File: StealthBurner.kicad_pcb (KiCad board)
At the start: 2 copper layers, 44.9 x 31.7 mm, 14 parts, among them J1 PROBE, J2 E-Step, J3 HE, J4 HET, J5 FS, J6 HEF, J7 PCF, J8 LED, J9 MCU, M1 Mount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

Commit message: 修改设计规范
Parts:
- moved J1 2.13 mm to (154.1, 107.2)
- moved D1 0.43 mm to (151.3, 102.7)
- moved G*** 0.25 mm to (152.7, 98.6)
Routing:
- net +24V: track 18.6 -> 16.4 mm
- net /HET: track 43.3 -> 44.3 mm
- net GNDA: track 56.3 -> 57.3 mm
- net /A-: track 8.05 -> 7.49 mm

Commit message: 重新设计 PCB
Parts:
- D1: footprint Diode_THT:D_DO-34_SOD68_P2.54mm_Vertical_AnodeUp -> Diode_THT:D_DO-35_SOD27_P2.54mm_Vertical_AnodeUp
- M1, M2: value Mount -> M3_hole; footprint MountingHole:MountingHole_3.2mm_M3_ISO7380_Pad -> MountingHole:MountingHole_3.2mm_M3_User
- moved J1 20.4 mm to (136.3, 97.3), turned to -90 degrees
- moved M1 19.7 mm to (148.0, 99.2)
- moved M2 15.3 mm to (136.0, 112.0)
- moved J3 14.9 mm to (152.6, 106.1), turned to 90 degrees
- moved D1 11.6 mm to (139.9, 100.4), turned to 90 degrees
- moved G*** 1.74 mm to (154.2, 97.8)
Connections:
- J9 pad 14: /P_SIG -> /HE-
- J9 pad 15: /FS -> /HE+
- J9 pad 4: /HE- -> /P_SIG
- J9 pad 5: /HE+ -> /FS
- J9 pad 8: /HEF -> /PCF
- J9 pad 9: /PCF -> /HEF
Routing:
- net /HEF: track 79.6 -> 37.0 mm
- net /PCF: track 68.6 -> 36.5 mm, vias 1 -> 0
- net /HE-: track 26.8 -> 3.26 mm
- net /P_SIG: track 5.35 -> 25.1 mm
- net /HE+: track 25.4 -> 6.37 mm
- net /DATA: track 57.6 -> 40.6 mm
- net /V_FAN: track 47.4 -> 64.1 mm
- net +24V: track 16.4 -> 26.9 mm
- net /HET: track 44.3 -> 36.9 mm
- net +5V: track 39.9 -> 32.9 mm
- net /FS: track 33.2 -> 37.9 mm
- net /CBT: track 36.1 -> 40.6 mm, vias 0 -> 2
- net GNDA: track 57.3 -> 55.3 mm
- net Net-(D1-Pad1): track 4.87 -> 4.08 mm
- net GND: vias 10 -> 0
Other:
- board size 44.9 x 31.7 mm -> 45 x 31.5 mm
- board text removed: "CBT"
- board text removed: "Controller"
- board text removed: "E-STEP"
- board text removed: "FS"
- board text removed: "HE"
- board text removed: "HEF"
- board text removed: "HET"
- board text removed: "NEO"
- board text removed: "PCF"
- board text removed: "PROBE"

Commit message: 更新到 Beta2
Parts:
- moved G*** 1.25 mm to (153.0, 98.0)
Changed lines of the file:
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@@
     (title "StealthBurner Toolhead PCB")
     (date "2022-05-24")
-    (rev "Bata0")
+    (rev "Bata1")
     (company "LassiCat Organization")
     (comment 1 "Auther: CharlieYu")
@@
     (property "Sheetname" "")
     (attr smd)
-    (fp_text reference "TH1" (at 0 1.75874) (layer "F.SilkS")
+    (fp_text reference "TH1" (at -3.082812 0.004398) (layer "F.SilkS")
       (effects (font (size 1 1) (thickness 0.15)))
     )
@@
     (property "Sheetname" "")
     (attr through_hole)
-    (fp_text reference "D1" (at 0.41 1.8 90) (layer "F.SilkS")
+    (fp_text reference "D1" (at -2.2 0) (layer "F.SilkS")
       (effects (font (size 1 1) (thickness 0.15)))
     )
@@
       (effects (font (size 1 1) (thickness 0.15)))
     )
-    (fp_text user "A" (at 4.34 0 90) (layer "F.SilkS")
-      (effects (font (size 1 1) (thickness 0.15)))
-    )
-    (fp_text user "A" (at 4.34 0 90) (layer "F.Fab")
-      (effects (font (size 1 1) (thickness 0.15)))
-    )
-    (fp_text user "${REFERENCE}" (at 1.27 -2.326371 90) (layer "F.Fab")
+    (fp_text user "A" (at 4.34 0 90) (layer "F.SilkS") hide
+      (effects (font (size 1 1) (thickness 0.15)))
+    )
+    (fp_text user "A" (at 4.34 0 90) (layer "F.Fab") hide
+      (effects (font (size 1 1) (thickness 0.15)))
+    )
+    (fp_text user "${REFERENCE}" (at 1.27 -2.326371 90) (layer "F.Fab") hide
       (effects (font (size 1 1) (thickness 0.15)))
     )
@@
     (tags "mounting hole 3.2mm no annular m3")
     (attr exclude_from_pos_files exclude_from_bom)
-    (fp_text reference "M2" (at 0 -4.2) (layer "F.SilkS")
-      (effects (font (size 1 1) (thickness 0.15)))
-    )
-    (fp_text value "M3_hole" (at 0 4.2) (layer "F.Fab")
-      (effects (font (size 1 1) (thickness 0.15)))
-    )
-    (fp_text user "${REFERENCE}" (at 0 0) (layer "F.Fab")
-      (effects (font (size 1 1) (thickness 0.15)))
-    )
-    (fp_circle (center 0 0) (end 2.54 0) (layer "Cmts.User") (width 0.15) (fill none))
-    (fp_circle (center 0 0) (end 2.54 0) (layer "F.CrtYd") (width 0.05) (fill none))
+    (fp_text reference "M2" (at 0 -4.2) (layer "F.SilkS") hide
+      (effects (font (size 1 1) (thickness 0.15)))
+    )
+    (fp_text value "M3_hole" (at 0 4.2) (layer "F.Fab") hide
+      (effects (font (size 1 1) (thickness 0.15)))
+    )
+    (fp_text user "${REFERENCE}" (at 0 0) (layer "F.Fab") hide
+      (effects (font (size 1 1) (thickness 0.15)))
+    )
+    (fp_circle (center 0 0) (end 2.05 0) (layer "F.SilkS") (width 0.75) (fill none))
+    (fp_circle (center 0 0) (end 1.6 0) (layer "Cmts.User") (width 0.1) (fill none))
+    (fp_circle (center 0 0) (end 1.6 0) (layer "F.CrtYd") (width 0.1) (fill none))
     (pad "" np_thru_hole circle (at 0 0) (size 3.2 3.2) (drill 3.2) (layers *.Cu *.Mask))
   )
@@
     (tags "mounting hole 3.2mm no annular m3")
     (attr exclude_from_pos_files exclude_from_bom)
-    (fp_text reference "M1" (at 0 -4.2) (layer "F.SilkS")
-      (effects (font (size 1 1) (thickness 0.15)))
-    )
-    (fp_text value "M3_hole" (at 0 4.2) (layer "F.Fab")
-      (effects (font (size 1 1) (thickness 0.15)))
-    )
-    (fp_text user "${REFERENCE}" (at 0 0) (layer "F.Fab")
-      (effects (font (size 1 1) (thickness 0.15)))
-    )
-    (fp_circle (center 0 0) (end 2.54 0) (layer "Cmts.User") (width 0.15) (fill none))
-    (fp_circle (center 0 0) (end 2.54 0) (layer "F.CrtYd") (width 0.05) (fill none))
+    (fp_text reference "M1" (at 0 -4.2) (layer "F.SilkS") hide
+      (effects (font (size 1 1) (thickness 0.15)))
+    )
+    (fp_text value "M3_hole" (at 0 4.2) (layer "F.Fab") hide
+      (effects (font (size 1 1) (thickness 0.15)))
+    )
+    (fp_text user "${REFERENCE}" (at 0 0) (layer "F.Fab") hide
+      (effects (font (size 1 1) (thickness 0.15)))
+    )
+    (fp_circle (center 0 0) (end 2.05 0) (layer "F.SilkS") (width 0.75) (fill none))
+    (fp_circle (center 0 0) (end 1.6 0) (layer "Cmts.User") (width 0.1) (fill none))
+    (fp_circle (center 0 0) (end 1.6 0) (layer "F.CrtYd") (width 0.1) (fill none))
     (pad "" np_thru_hole circle (at 0 0) (size 3.2 3.2) (drill 3.2) (layers *.Cu *.Mask))
   )
@@
   )
   (footprint "Logos:voron_logo_hex" (layer "F.Cu")
-    (at 154.24 97.81)
+    (at 153 98)
     (attr board_only exclude_from_pos_files exclude_from_bom)
     (fp_text reference "G***" (at 0 0) (layer "F.SilkS") hide
@@
     )
   )
-  (gr_circle (center 148 99.23) (end 151 99.23) (layer "F.SilkS") (width 0.1) (fill solid))
-  (gr_circle (center 136 112) (end 139 112) (layer "F.SilkS") (width 0.1) (fill solid))
   (gr_line (start 125.5 90.5) (end 125.5 115.5) (layer "Edge.Cuts") (width 0.1))
   (gr_line (start 170.5 119) (end 170.5 90.5) (layer "Edge.Cuts") (width 0.1))
@@
   (group "" (id 138ee650-507a-4b6c-aa52-9a524f6554fc)
     (members
-      3c19eee8-8ef9-4c6e-b5af-9f26817e96ee
-      88c53001-83db-453f-916c-506f3ad8d7eb
       d2e33ac6-8ba1-45b4-a4e6-6e1f013e565c
       d51818f7-3221-478a-8396-f76ef6cf744f

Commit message: 更新 Gerber 文件以及 BOM 表
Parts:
- added REF**: LassiCat, Logos:LassiCat, F.Cu at (134.0, 106.5)
- moved G*** 1.31 mm to (153.4, 99.2)
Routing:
- net /DATA: track 40.6 -> 42.7 mm
- net /PCF: track 36.5 -> 38.0 mm
- net /CBT: track 40.6 -> 39.3 mm
- net /HEF: track 37.0 -> 36.0 mm
- net GNDA: track 55.3 -> 54.6 mm
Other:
- board text added: "CharlieYu"
- board text added: "LassiCat"

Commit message: 添加丝印
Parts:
- moved D1 4.59 mm to (143.7, 97.8), turned to -90 degrees
- moved J1 2.08 mm to (138.3, 97.3)
- moved J9 0.15 mm to (161.4, 92.8)
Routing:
- net /P_SIG: track 25.1 -> 20.3 mm
- net Net-(D1-Pad1): track 4.08 -> 5.97 mm
- net +24V: track 26.9 -> 26.2 mm
- net GND: vias 0 -> 15
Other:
- board text added: "Controller"
- board text added: "FS"
- board text added: "HE"
- board text added: "HEF"
- board text added: "HET"
- board text added: "NEO"
- board text added: "PCF"
- board text added: "PROBE"
- board text added: "STEP"

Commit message: 添加 BOM
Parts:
- renumbered REF** to L1, G*** to L2
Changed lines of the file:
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@@
   (footprint "Logos:LassiCat" (layer "F.Cu")
     (at 134 106.5)
-    (fp_text reference "REF**" (at -4.1 -9.66 unlocked) (layer "F.SilkS") hide
+    (attr board_only exclude_from_pos_files exclude_from_bom)
+    (fp_text reference "L1" (at -4.1 -9.66 unlocked) (layer "F.SilkS") hide
       (effects (font (size 1 1) (thickness 0.15)))
     )
     (fp_text value "LassiCat" (at -0.25 4.69 unlocked) (layer "F.Fab") hide
-      (effects (font (size 1 1) (thickness 0.15)))
-    )
-    (fp_text user "${REFERENCE}" (at 0.53 7.14 unlocked) (layer "F.Fab") hide
       (effects (font (size 1 1) (thickness 0.15)))
     )
@@
     (at 153.44 99.23)
     (attr board_only exclude_from_pos_files exclude_from_bom)
-    (fp_text reference "G***" (at 0 0) (layer "F.SilkS") hide
+    (fp_text reference "L2" (at 0 0) (layer "F.SilkS") hide
       (effects (font (size 1.524 1.524) (thickness 0.3)))
     )

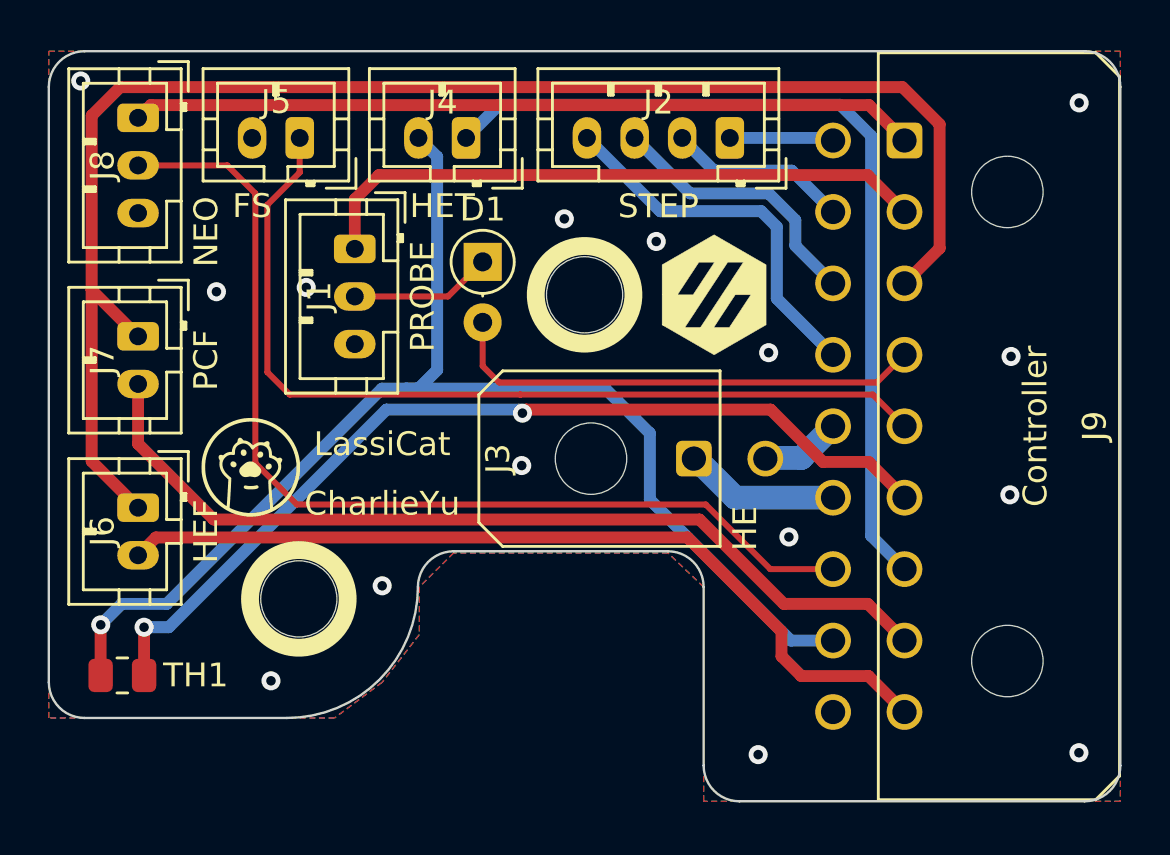
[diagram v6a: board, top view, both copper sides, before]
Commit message: 更新到 Beta2，优化探针接口位置，优化丝印
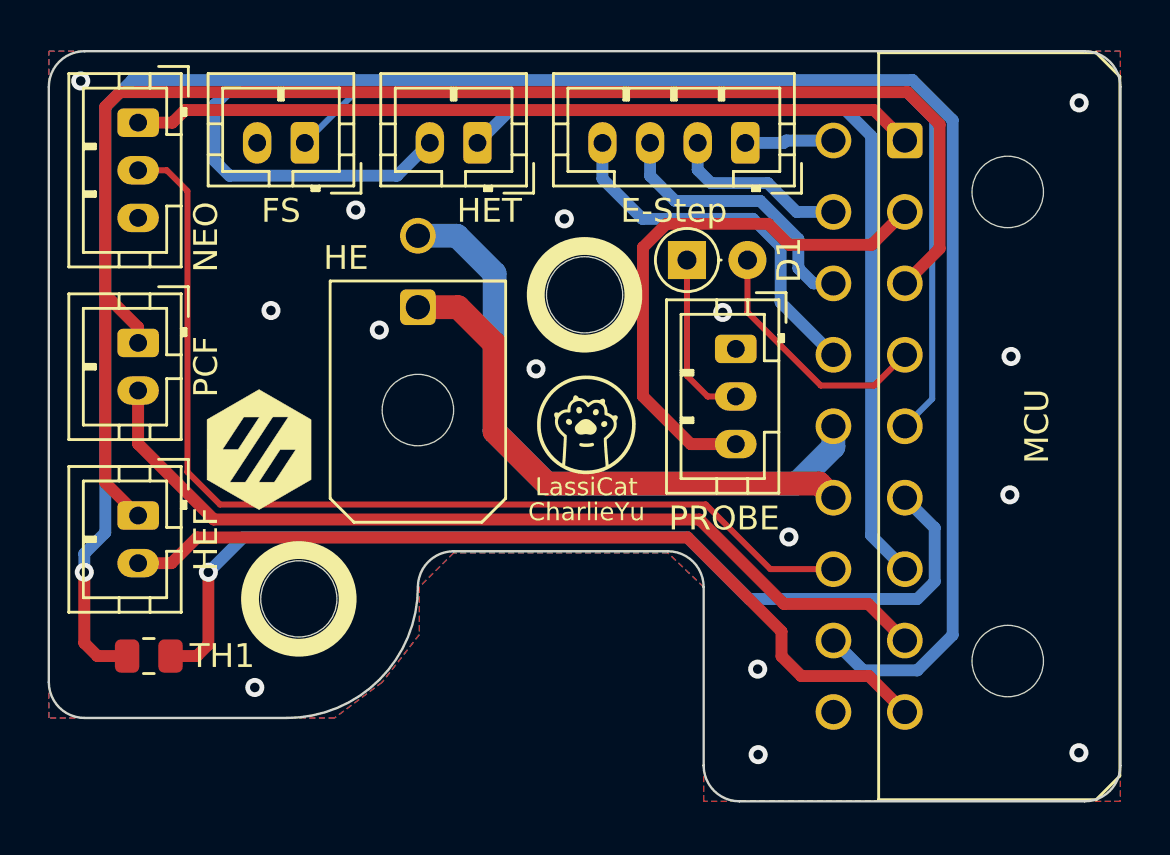
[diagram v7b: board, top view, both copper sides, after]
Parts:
- J8: value LED -> NEO
- L1: value LassiCat -> LassiCat Organization; footprint Logos:LassiCat -> Logos:lassicat
- moved L2 20.2 mm to (134.3, 105.7)
- moved J1 16.5 mm to (154.3, 101.5)
- moved L1 14.2 mm to (148.1, 104.7)
- moved J3 13.2 mm to (141.0, 99.8), turned to 180 degrees
- moved D1 8.58 mm to (152.3, 97.8), turned to 0 degrees
- moved TH1 1.38 mm to (129.7, 114.4)
- moved J2 0.68 mm to (154.8, 92.8)
- moved J4 0.52 mm to (143.5, 92.8)
- moved J6 0.33 mm to (129.2, 108.5)
- moved J5 0.30 mm to (136.2, 92.8)
- moved J7 0.28 mm to (129.2, 101.2)
- moved J8 0.20 mm to (129.2, 92.0)
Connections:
- J1 pad 1: +24V -> GND
- J1 pad 3: GND -> +24V
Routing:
- net GNDA: track 54.7 -> 103.1 mm
- net /HE-: track 3.40 -> 27.2 mm
- net /HE+: track 6.52 -> 22.9 mm
- net /P_SIG: track 20.3 -> 10.6 mm
- net +24V: track 26.2 -> 23.3 mm
- net /FS: track 38.1 -> 40.9 mm
- net /CBT: track 39.5 -> 41.4 mm, vias 2 -> 1
- net Net-(D1-Pad1): track 5.97 -> 7.27 mm
- net /A+: track 4.54 -> 3.74 mm
- net /V_FAN: track 64.1 -> 63.5 mm
- net /HET: track 36.9 -> 36.3 mm
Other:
- board text removed: "Controller"
- board text removed: "FS"
- board text removed: "HE"
- board text removed: "HEF"
- board text removed: "HET"
- board text removed: "NEO"
- board text removed: "PCF"
- board text removed: "PROBE"
- board text removed: "STEP"

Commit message: 微调丝印
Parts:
- L1: footprint Logos:lassicat -> Logos_User:LassiCat_Logo
- L2: value LOGO -> Voron Hex; footprint Logos:voron_logo_hex -> Logos_User:Voron_Logo_Hex
- M1, M2: footprint MountingHole:MountingHole_3.2mm_M3_User -> MountingHole_User:MountingHole_3.2mm_M3_User
- moved J3 0.22 mm to (140.9, 99.6)
- moved TH1 0.21 mm to (129.5, 114.4)
